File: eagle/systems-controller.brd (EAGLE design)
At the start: 80 x 40 mm, 52 parts, among them IC1 MK20DX256VLH7, IC2 MKL02Z32VFG4, IC3 TPS6214XRGT, J1 SIG, J2 PWR, J3 GND, Q1 FA-238, Q2 PMV20ENR, Q3 PMV20ENR, Q4 PMV20ENR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

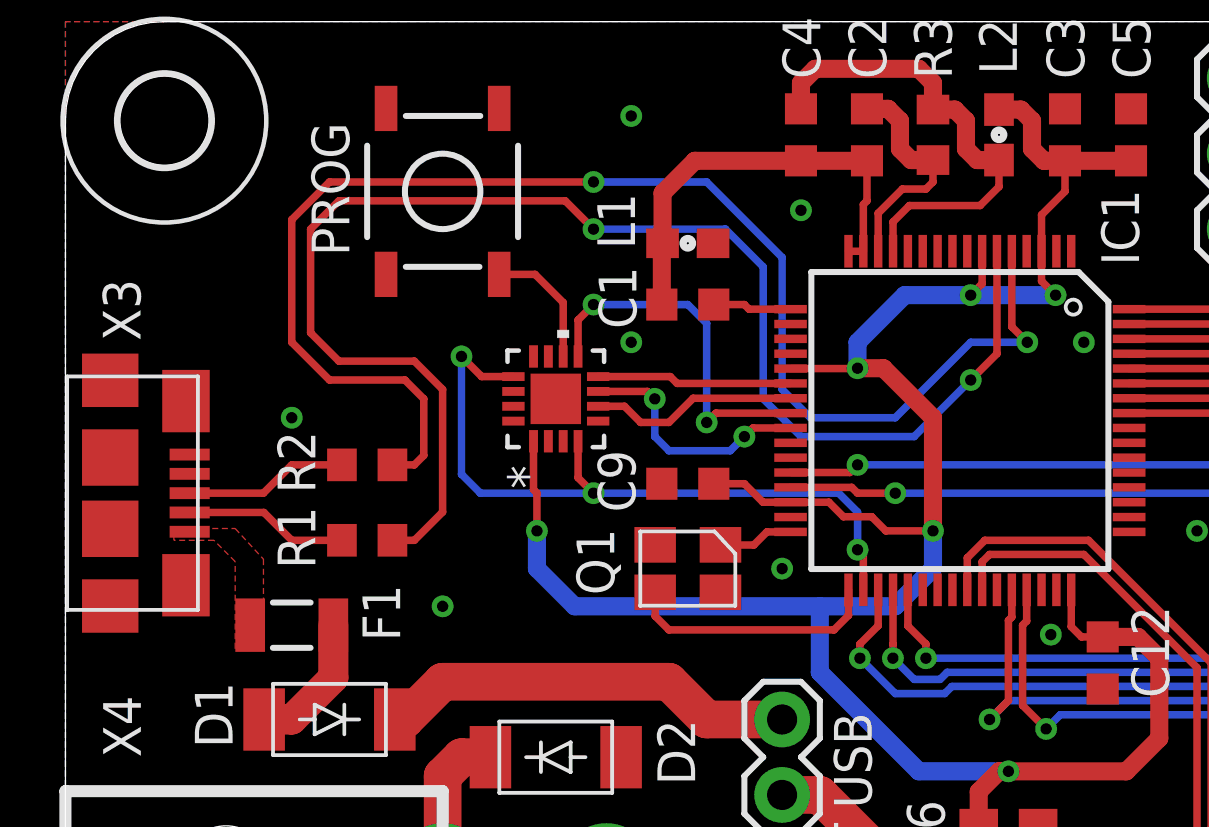
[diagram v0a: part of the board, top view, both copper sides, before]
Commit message: fixed reversed usb connector footprint
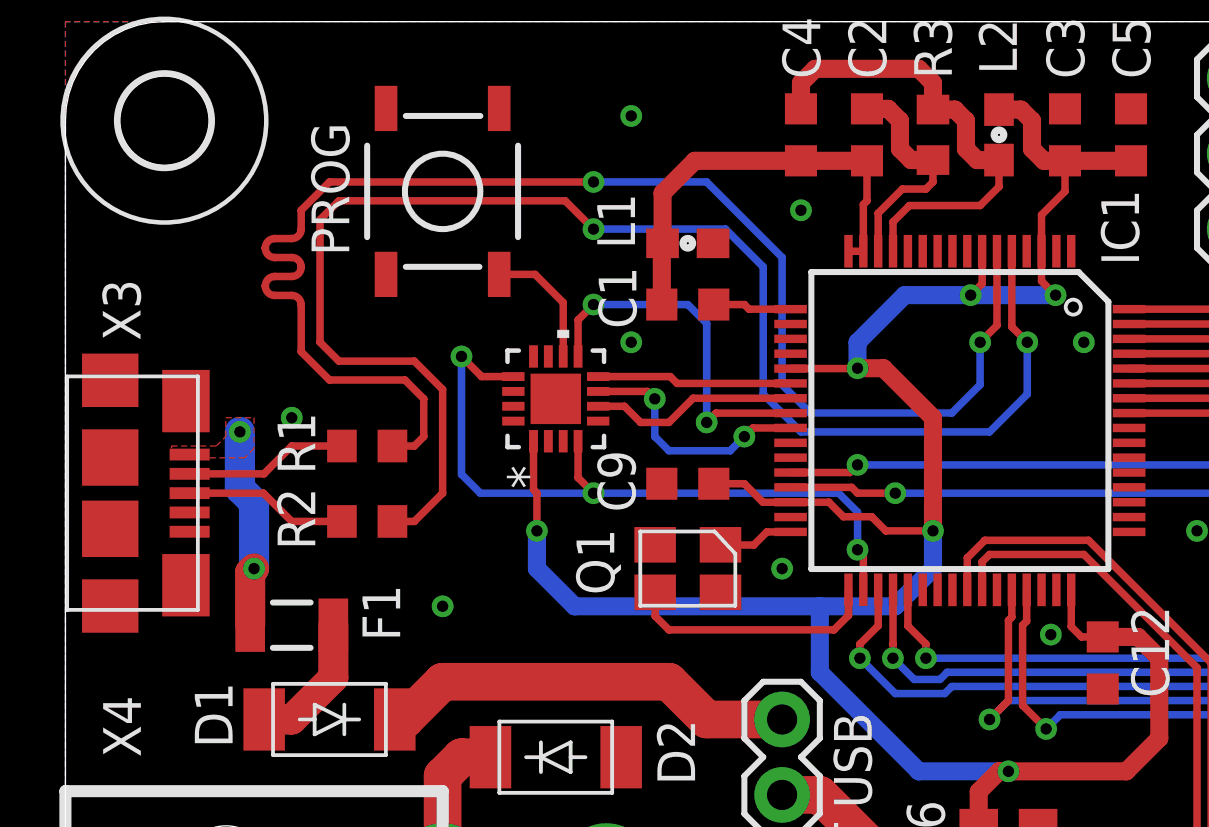
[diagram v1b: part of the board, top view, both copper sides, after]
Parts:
- moved R1 3.18 mm to (10.2, 25.7)
- moved R2 1.91 mm to (10.2, 23.2)
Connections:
- net GND: now also X3.5; no longer X3.1
- net N$6: now also X3.2; no longer X3.4
- net VBUS: now also X3.1; no longer X3.5
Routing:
- net VBUS: track 0.00 -> 6.76 mm, vias 0 -> 2
- net N$9: track 48.0 -> 49.9 mm
- net N$7: track 48.9 -> 49.5 mm
